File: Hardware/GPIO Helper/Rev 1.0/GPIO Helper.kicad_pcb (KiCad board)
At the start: 2 copper layers, 100 x 50 mm, 42 parts, among them J1 PORT A, J2 PORT B, SW1 PA7, SW2 PA6, SW3 PA5, SW4 PA4, SW5 PA3, SW6 PA2, SW7 PA1, SW8 PA0

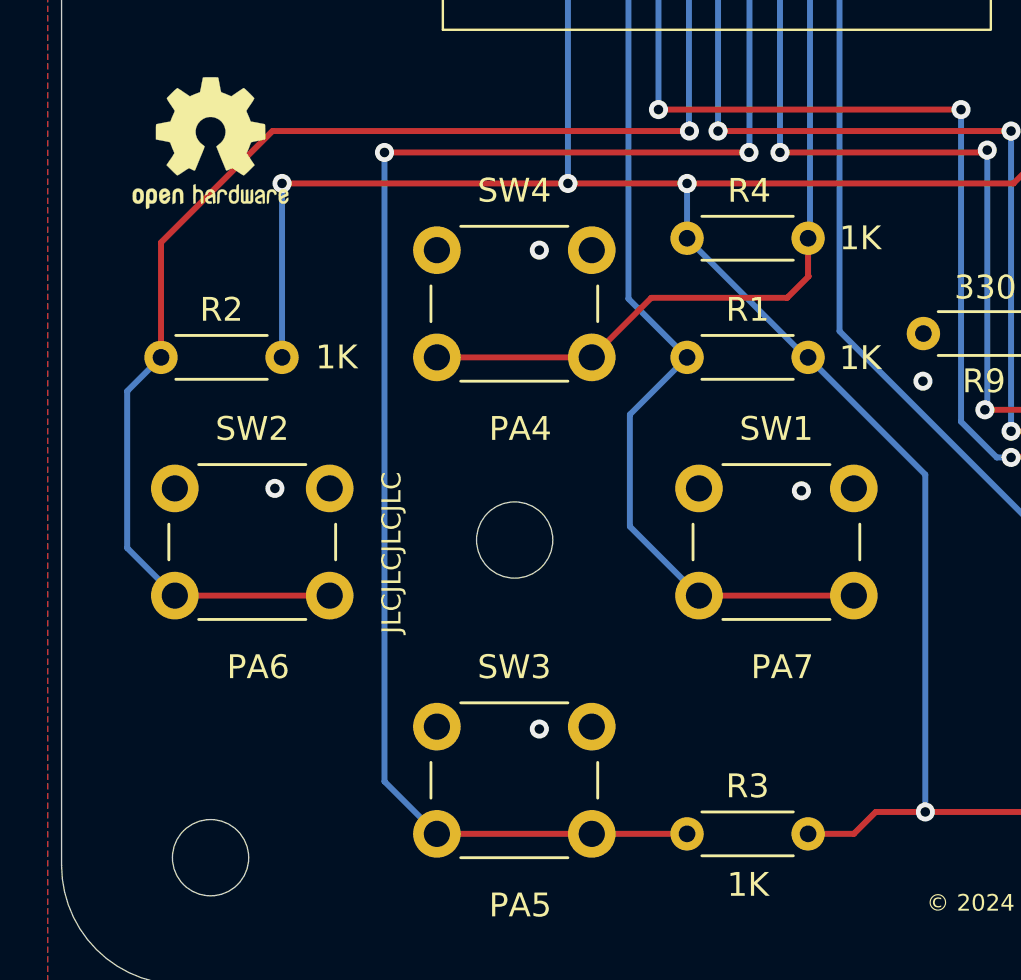
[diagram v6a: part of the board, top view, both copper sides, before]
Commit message: Fix GPIO Helper button alignment
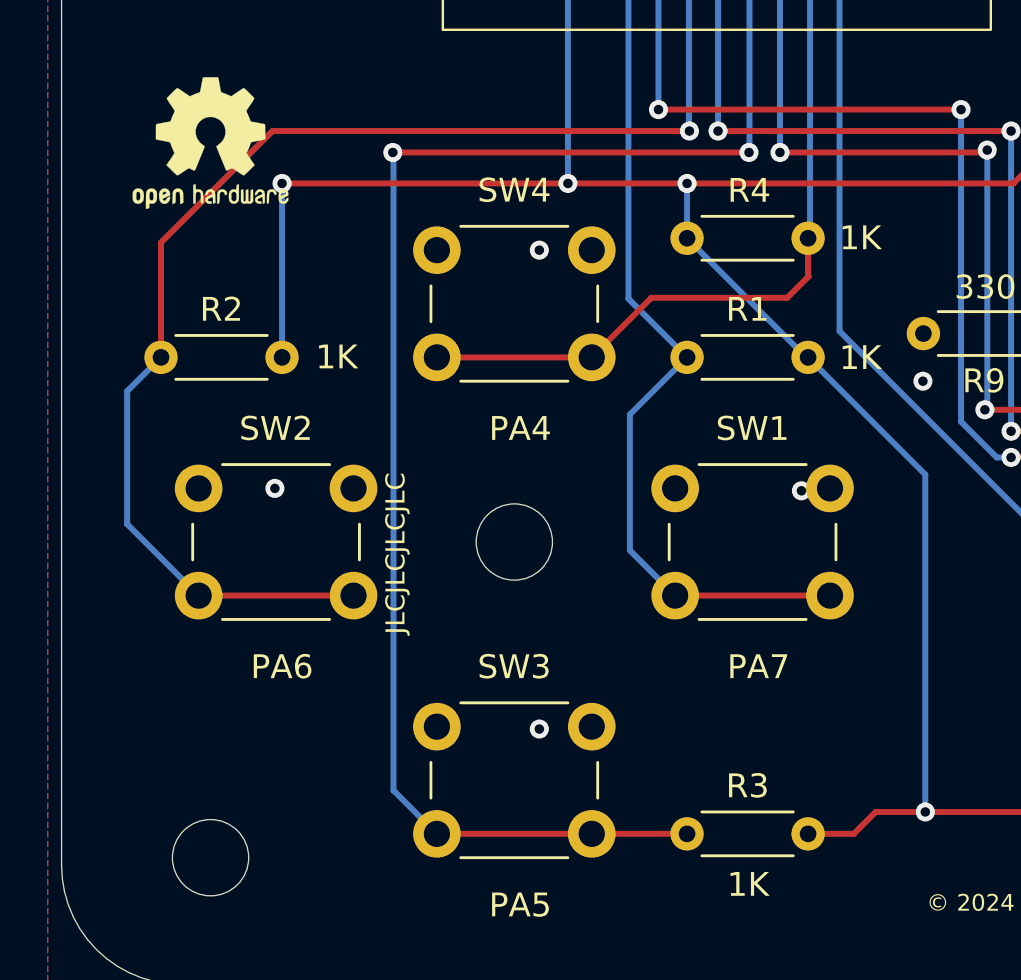
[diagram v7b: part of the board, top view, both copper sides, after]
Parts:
- moved SW1 1.00 mm to (90.8, 112.3)
- moved SW2 1.00 mm to (70.8, 112.3)
- moved H5 0.09 mm to (84.1, 114.6)
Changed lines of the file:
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@@
 	(footprint "MountingHole:MountingHole_3.2mm_M3"
 		(layer "F.Cu")
-		(at 84.06555 114.48)
+		(at 84.05155 114.564)
 		(descr "Mounting Hole 3.2mm, no annular, M3")
 		(tags "mounting hole 3.2mm no annular m3")
@@
 	(footprint "Button_Switch_THT:SW_PUSH_6mm"
 		(layer "F.Cu")
-		(at 91.8011 112.3136)
+		(at 90.8011 112.3136)
 		(descr "Generic 6mm SW tactile push button")
 		(tags "tact sw push 6mm")
@@
 	(footprint "Button_Switch_THT:SW_PUSH_6mm"
 		(layer "F.Cu")
-		(at 69.8011 112.3136)
+		(at 70.8011 112.3136)
 		(descr "Generic 6mm SW tactile push button")
 		(tags "tact sw push 6mm")
@@
 	)
 	(gr_text "JLCJLCJLCJLC"
-		(at 78.9011 115.0136 90)
+		(at 79.07 115.04 90)
 		(layer "F.SilkS")
 		(effects
@@
 	(segment
 		(start 93.9011 98.2136)
-		(end 78.6011 98.2136)
+		(end 78.95 98.2136)
 		(width 0.25)
 		(layer "F.Cu")
@@
 	)
 	(via
-		(at 78.6011 98.2136)
+		(at 78.95 98.2136)
 		(size 0.8)
 		(drill 0.4)
@@
 	)
 	(segment
+		(start 78.98 98.2436)
+		(end 78.98 124.9925)
+		(width 0.25)
+		(layer "B.Cu")
+		(net 19)
+	)
+	(segment
 		(start 93.9211 98.1936)
 		(end 93.9011 98.2136)
@@
 	)
 	(segment
-		(start 78.6011 124.6136)
-		(end 80.8011 126.8136)
+		(start 93.9211 89.8136)
+		(end 93.9211 98.1936)
 		(width 0.25)
 		(layer "B.Cu")
@@
 	)
 	(segment
-		(start 78.6011 98.2136)
-		(end 78.6011 124.6136)
+		(start 78.95 98.2136)
+		(end 78.98 98.2436)
 		(width 0.25)
 		(layer "B.Cu")
@@
 	)
 	(segment
-		(start 93.9211 89.8136)
-		(end 93.9211 98.1936)
+		(start 78.98 124.9925)
+		(end 80.8011 126.8136)
 		(width 0.25)
 		(layer "B.Cu")
@@
 	)
 	(segment
-		(start 91.8011 116.8136)
-		(end 98.3011 116.8136)
+		(start 90.8011 116.8136)
+		(end 97.3011 116.8136)
 		(width 0.25)
 		(layer "F.Cu")
@@
 	)
 	(segment
-		(start 88.9011 109.2136)
-		(end 88.9011 113.9136)
+		(start 90.8011 116.8136)
+		(end 88.9011 114.9136)
 		(width 0.25)
 		(layer "B.Cu")
@@
 	)
 	(segment
-		(start 88.8411 104.3536)
-		(end 91.3011 106.8136)
+		(start 88.9011 114.9136)
+		(end 88.9011 109.2136)
 		(width 0.25)
 		(layer "B.Cu")
@@
 	)
 	(segment
-		(start 88.8411 89.8136)
-		(end 88.8411 104.3536)
+		(start 88.9011 109.2136)
+		(end 91.3011 106.8136)
 		(width 0.25)
 		(layer "B.Cu")
@@
 	)
 	(segment
-		(start 91.3011 106.8136)
-		(end 88.9011 109.2136)
+		(start 88.8411 104.3536)
+		(end 91.3011 106.8136)
 		(width 0.25)
 		(layer "B.Cu")
@@
 	)
 	(segment
-		(start 88.9011 113.9136)
-		(end 91.8011 116.8136)
+		(start 88.8411 89.8136)
+		(end 88.8411 104.3536)
 		(width 0.25)
 		(layer "B.Cu")
@@
 	)
 	(segment
-		(start 69.8011 116.8136)
-		(end 76.3011 116.8136)
+		(start 91.4011 97.3136)
+		(end 73.9011 97.3136)
 		(width 0.25)
 		(layer "F.Cu")
@@
 	)
 	(segment
-		(start 91.4011 97.3136)
-		(end 73.9011 97.3136)
+		(start 69.2211 101.9936)
+		(end 69.2211 106.8136)
 		(width 0.25)
 		(layer "F.Cu")
@@
 	)
 	(segment
-		(start 69.2211 101.9936)
-		(end 69.2211 106.8136)
+		(start 70.8011 116.8136)
+		(end 77.3011 116.8136)
 		(width 0.25)
 		(layer "F.Cu")
@@
 	)
 	(segment
-		(start 69.8011 116.8136)
-		(end 67.8011 114.8136)
+		(start 67.8011 108.2336)
+		(end 67.8011 113.8136)
 		(width 0.25)
 		(layer "B.Cu")
@@
 	)
 	(segment
-		(start 67.8011 114.8136)
+		(start 69.2211 106.8136)
 		(end 67.8011 108.2336)
 		(width 0.25)
@@
 	)
 	(segment
-		(start 67.8011 108.2336)
-		(end 69.2211 106.8136)
+		(start 91.3811 89.8136)
+		(end 91.3811 97.2936)
 		(width 0.25)
 		(layer "B.Cu")
@@
 	)
 	(segment
-		(start 91.3811 89.8136)
-		(end 91.3811 97.2936)
+		(start 67.8011 113.8136)
+		(end 70.8011 116.8136)
 		(width 0.25)
 		(layer "B.Cu")
